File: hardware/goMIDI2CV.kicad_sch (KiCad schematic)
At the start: 21 parts, among them J1 HDR-16PIN, J2 MIDI DIN-5, J3 PJ301M-12, J4 PJ301M-12, J5 PJ301M-12, U1 ATtiny85, U2 LM324, U3 6N138

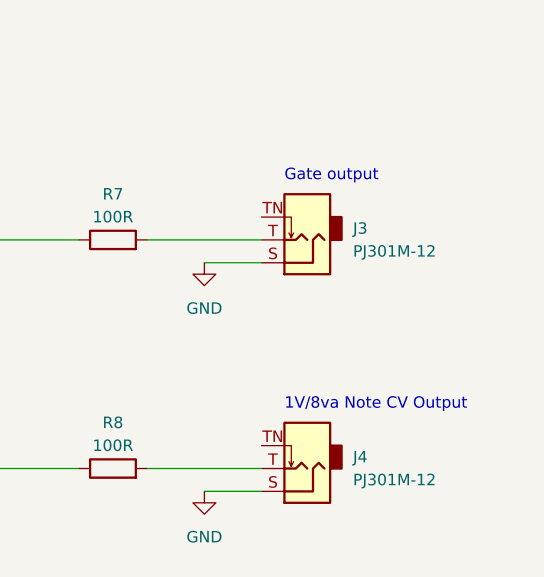
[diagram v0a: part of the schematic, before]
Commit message: replace files via upload
fixed labels on gate and note cv outputs
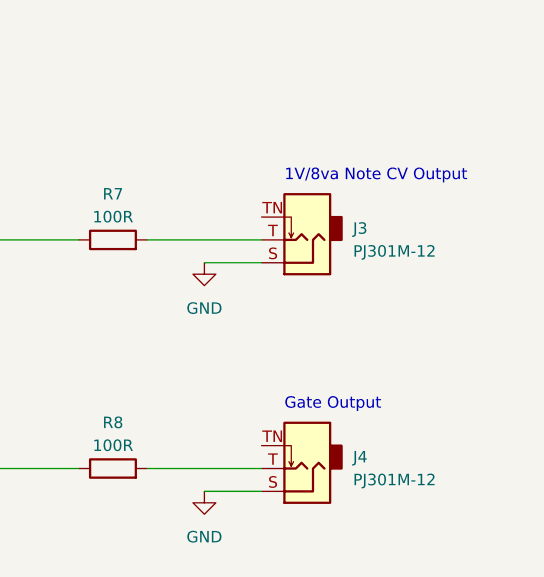
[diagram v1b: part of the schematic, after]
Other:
- note added: "Gate Output"
- note removed: "Gate output"
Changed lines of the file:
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@@
     (effects (font (size 1.27 1.27)) (justify left bottom))
   )
-  (text "Gate output" (at 231.14 72.39 0)
+  (text "1V/8va Note CV Output" (at 231.14 72.39 0)
     (effects (font (size 1.27 1.27)) (justify left bottom))
   )
@@
     (effects (font (size 1.27 1.27)) (justify left bottom))
   )
-  (text "1V/8va Note CV Output" (at 231.14 97.79 0)
+  (text "Gate Output" (at 231.14 97.79 0)
     (effects (font (size 1.27 1.27)) (justify left bottom))
   )
